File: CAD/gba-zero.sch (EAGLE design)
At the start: 35 parts, among them IC5 APX803, Q2 BSS138

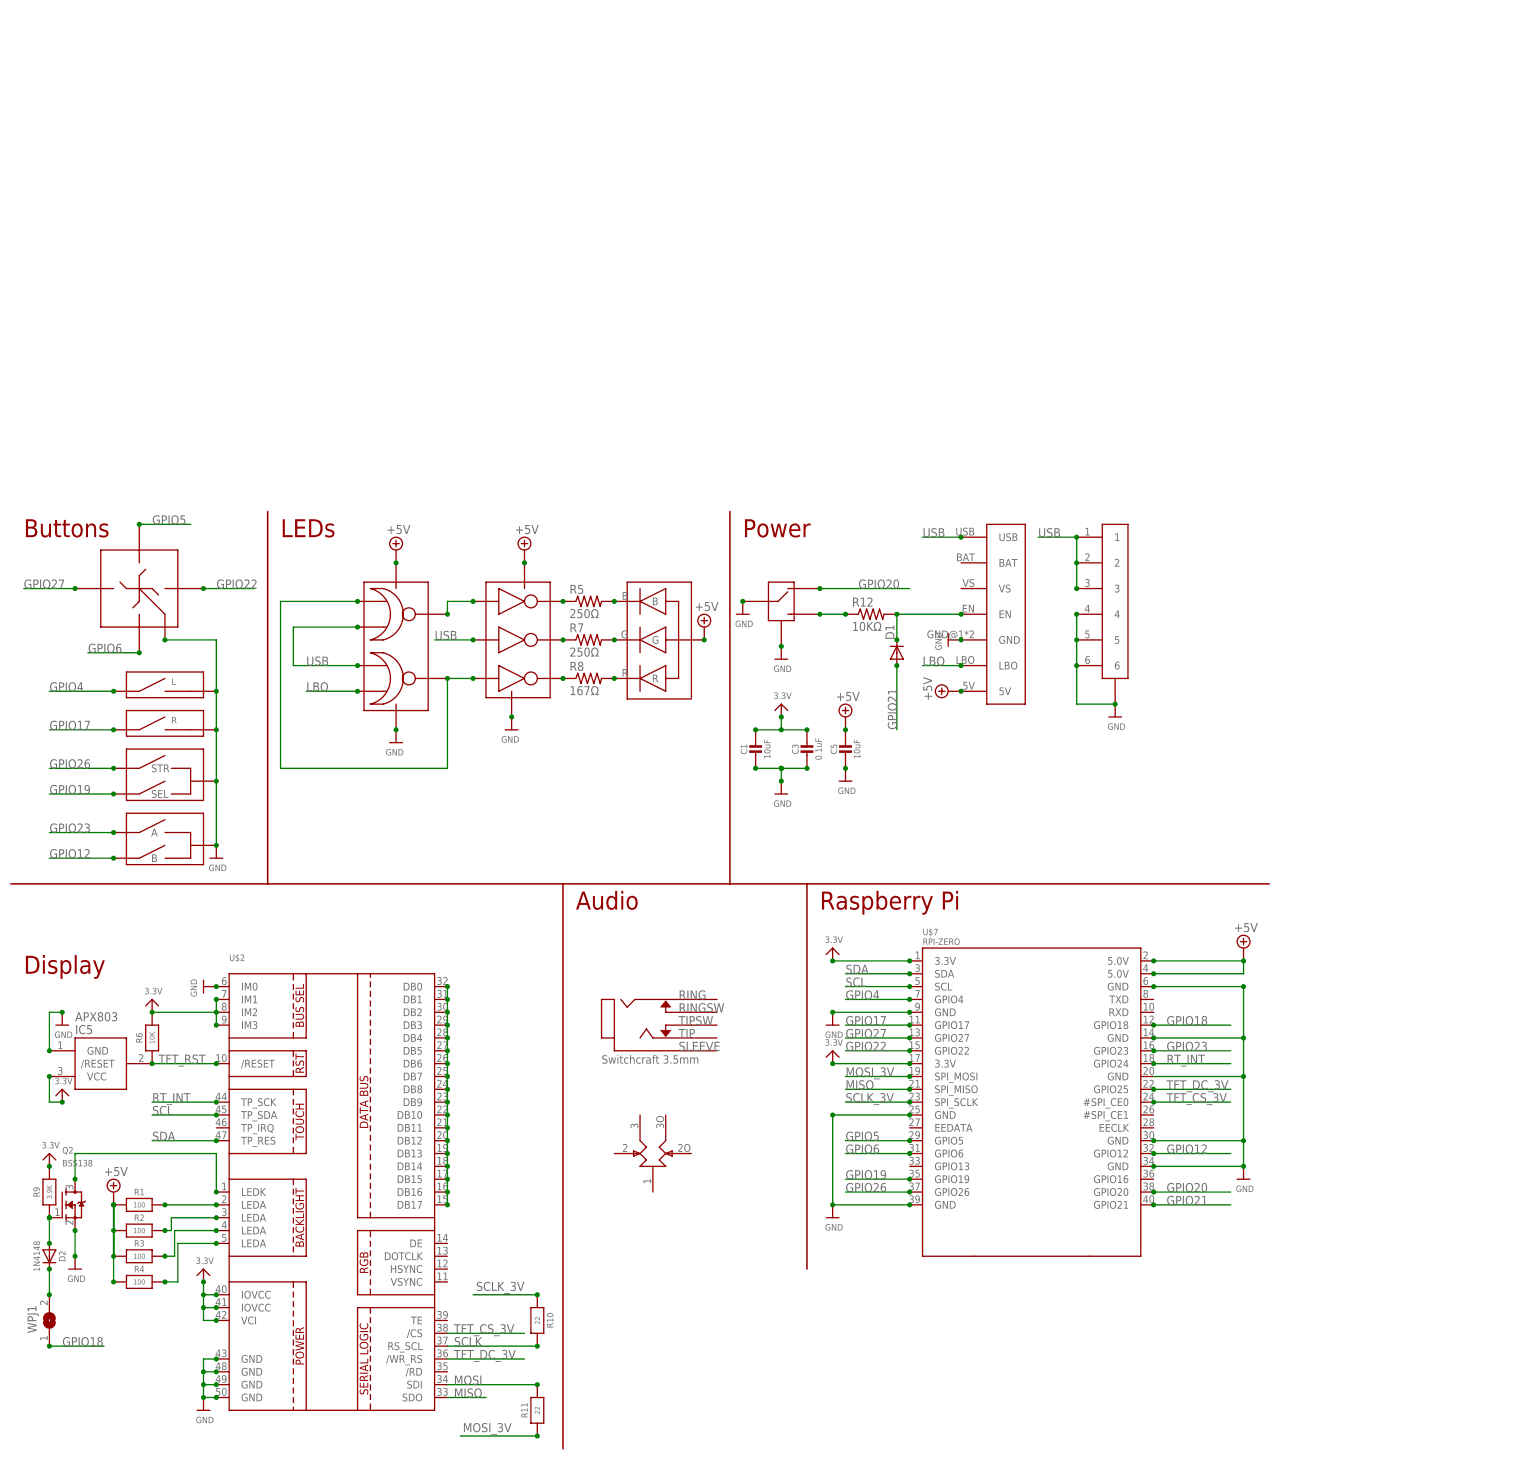
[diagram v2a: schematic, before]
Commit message: Added audio to schematic
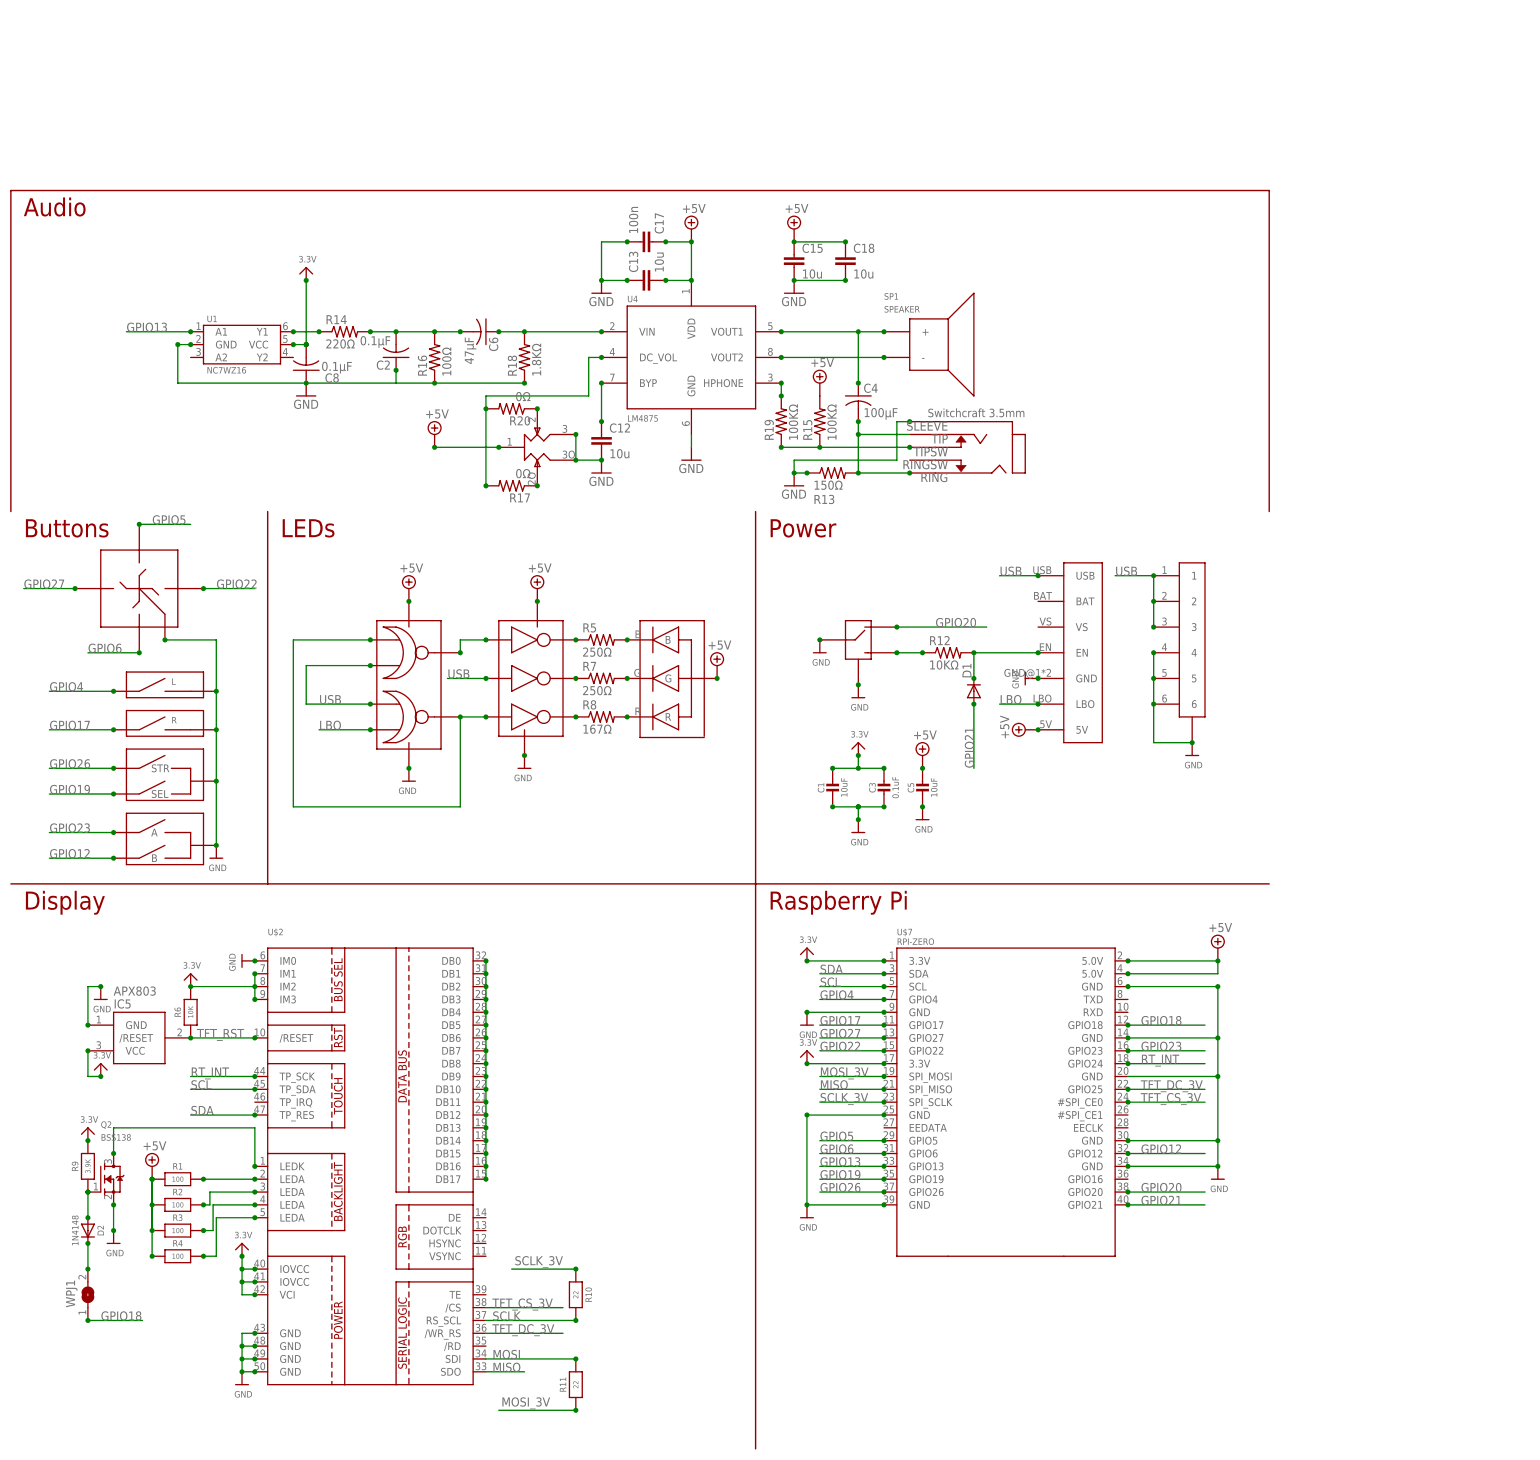
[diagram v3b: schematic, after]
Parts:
- removed U$15: RK10J12E0A0A, gba-zero-parts:RK10J12E0A0A
- removed U$22: SWTCHCRFT_3.5JACK5-JACK-SMD, gba-zero-parts:SWTCHCRFT_3.5JACK5-JACK-SMD
- added C12, C13, C15, C18: 10u, rcl:C-EUC0805
- added C17: 100n, rcl:C-EUC0805
- added C2, C8: 0.1μF, rcl:C-USC0603
- added C4: 100μF, rcl:C-USC0603
- added C6: 47μF, rcl:C-USC0603
- added R13: 150Ω, resistor:R-US_R0603
- added R14: 220Ω, resistor:R-US_R0603
- added R15, R19: 100KΩ, resistor:R-US_R0603
- added R16: 100Ω, resistor:R-US_R0603
- added R17, R20: 0Ω, resistor:R-US_R0603
- added R18: 1.8KΩ, resistor:R-US_R0603
- added SP1: SPEAKER, GBA:SPEAKER
- added U$16: SWTCHCRFT_3.5JACK5-JACK-SMD, gba-zero-parts:SWTCHCRFT_3.5JACK5-JACK-SMD
- added U$17: 10K, gba-zero-parts:RK10J12E0A0A
- added U1: NC7WZ16, fairchild:NC7WZ16
- added U4: LM4875, texas:LM4875
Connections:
- new net GPIO13: U$7.GPIO13, U1.A1
- new net N$19: C4.2, R13.2, U$16.2, U$16.3
- new net N$20: R14.1, U1.Y1
- new net N$21: C2.2, C6.2, R14.2, R16.2
- new net N$22: R15.1, R19.1, U$16.5
- new net N$23: R19.2, U4.HPHONE
- new net N$24: R17.1, U$17.2O
- new net N$25: R20.1, U$17.2
- new net N$26: R17.2, R20.2, U4.DC_VOL
- new net N$30: C6.1, R18.2, U4.VIN
- new net N$35: C12.1, U4.BYP
- new net N$36: C4.1, SP1.+, U4.VOUT1
- new net N$37: SP1.-, U4.VOUT2
- net +5V: now also C13.2, C15.1, C17.1, C18.1, R15.2, U$17.1, U4.VDD
- net 3.3V: now also C8.2, U1.VCC
- net GND: now also C12.2, C13.1, C15.2, C17.2, C18.2, C2.1, C8.1, R13.1, R16.1, R18.1, U$16.1, U$17.3, U$17.3O, U1.GND, U4.GND
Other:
- moved on the sheet: C1, C3, C5, D1, D2, IC5, Q2, R1, R10, R11, R12, R2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

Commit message: Lots of schematic cleanup
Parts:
- removed R13: 150Ω, resistor:R-US_R0603
- removed R14: 220Ω, resistor:R-US_R0603
- removed R15, R19: 100KΩ, resistor:R-US_R0603
- removed R16: 100Ω, resistor:R-US_R0603
- removed R18: 1.8KΩ, resistor:R-US_R0603
- added R21: 250, microbuilder:RESISTOR0805
- added R22, R23: 100K, microbuilder:RESISTOR0805
- added R24: 150, microbuilder:RESISTOR0805
- added WPJ4: 0, microbuilder:SOLDERJUMPERCLOSED
- C1, C3, C5: device microbuilder:CAP_CERAMIC0805-NOOUTLINE -> microbuilder:CAP_CERAMIC0805
- D1: value (none) -> IN4001
- R1, R10, R11, R2, R3, R4, R6, R9: device microbuilder:RESISTOR0805_NOOUTLINE -> microbuilder:RESISTOR0805
- R12: value 10KΩ -> 1.8K; device resistor:R-US_R0603 -> microbuilder:RESISTOR0805
- R17: value 0Ω -> 167; device resistor:R-US_R0603 -> microbuilder:RESISTOR0805
- R20: value 0Ω -> 250; device resistor:R-US_R0603 -> microbuilder:RESISTOR0805
- R5: value 250Ω -> 10K; device resistor:R-US_R0603 -> microbuilder:RESISTOR0805
- R7: value 250Ω -> 220; device resistor:R-US_R0603 -> microbuilder:RESISTOR0805
- R8: value 167Ω -> 100; device resistor:R-US_R0603 -> microbuilder:RESISTOR0805
- U$2: value (none) -> 50_PIN_CON
- U$7: device RPI-Zero:RPI-ZERO -> gba-zero-parts:RPI-ZERO
- WPJ1: value (none) -> 0
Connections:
- net GPIO12 renamed BTN_B
- net GPIO13 renamed AUD_PWM
- net GPIO17 renamed BTN_RS
- net GPIO18 renamed BKLT_PWM
- net GPIO19 renamed BTN_SEL
- net GPIO20 renamed PWR_SW_SEN
- net GPIO21 renamed PWR_EN_RPI
- net GPIO22 renamed BTN_R
- net GPIO23 renamed BTN_A
- net GPIO26 renamed BTN_STR
- net GPIO27 renamed BTN_L
- net GPIO4 renamed BTN_LS
- net GPIO5 renamed BTN_U
- net GPIO6 renamed BTN_D
- removed net 5.0V: C5.1, R1.1, R2.1, R3.1, R4.1, U$12.5V, U$42.VCC, U$43.VCC, U$44.VCC
- removed net N$19: C4.2, R13.2, U$16.2, U$16.3
- removed net N$24: R17.1, U$17.2O
- removed net N$25: R20.1, U$17.2
- new net BKLT: U$7.GPIO16, WPJ4.1
- new net RING: C4.2, R24.2, U$16.2, U$16.3
- new net RXD: U$10.3, U$7.RXD
- new net TXD: U$10.4, U$7.TXD
- net +5V: now also C5.P$1, R1.1, R2.1, R23.1, R3.1, R4.1, U$12.5V, U$42.VCC, U$43.VCC, U$44.VCC; no longer R15.2
- net 3.3V: now also C1.P$1, C3.P$1; no longer C1.1, C3.1
- net GND: now also C1.P$2, C3.P$2, C5.P$2, R12.2, R24.1, R8.2; no longer C1.2, C3.2, C5.2, R13.1, R16.1, R18.1, U$10.4
- net N$11: now also R20.2, U$43.2Y; no longer R8.1, U$43.3Y
- net N$12: now also R20.1, U$44.G; no longer R5.2, U$44.B
- net N$13: now also R21.2, U$43.1Y; no longer R7.2, U$44.G
- net N$14: now also R21.1, U$44.B; no longer R8.2, U$44.R
- net N$17: now also R5.2; no longer R12.1
- net N$18: now also R5.1; no longer R12.2
- net N$20: now also R7.2; no longer R14.1
- net N$21: now also R7.1, R8.1; no longer R14.2, R16.2
- net N$22: now also R22.2, R23.2; no longer R15.1, R19.1
- net N$23: now also R22.1; no longer R19.2
- net N$26: now also U$17.2; no longer R17.2, R20.2
- net N$30: now also R12.1; no longer R18.2
- net N$5: now also R17.2, U$43.3Y; no longer R5.1, U$43.1Y
- net N$6: now also WPJ4.2
- net N$8: now also R17.1, U$44.R; no longer R7.1, U$43.2Y
- net USB: no longer U$10.3
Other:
- moved on the sheet: C1, C2, C3, C5, C6, C8, D2, IC5, Q2, R1, R10, R11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

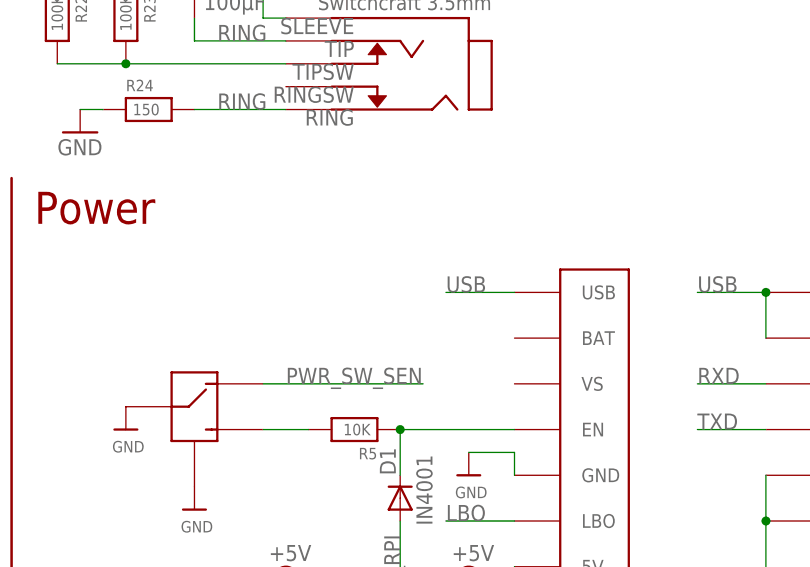
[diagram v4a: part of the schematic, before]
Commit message: Added JST battery connector
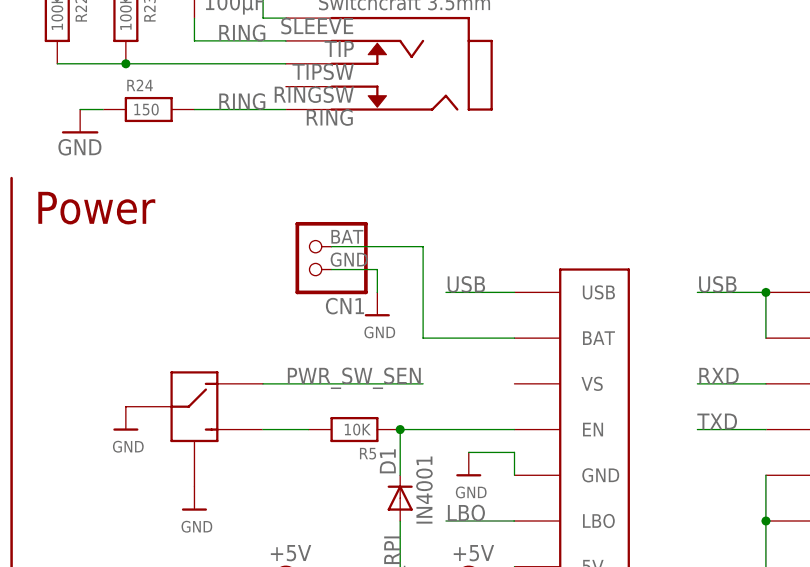
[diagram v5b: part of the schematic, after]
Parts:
- added CN1: (no value), gba-zero-parts:JST_2PIN
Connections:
- new net N$19: CN1.2, U$12.BAT
- net GND: now also CN1.1
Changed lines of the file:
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@@
 <setting verticaltext="up"/>
 </settings>
-<grid distance="0.1" unitdist="inch" unit="inch" style="lines" multiple="1" display="yes" altdistance="0.01" altunitdist="inch" altunit="inch"/>
+<grid distance="0.1" unitdist="inch" unit="inch" style="lines" multiple="1" display="no" altdistance="0.01" altunitdist="inch" altunit="inch"/>
 <layers>
 <layer number="1" name="Top" color="4" fill="1" visible="no" active="no"/>
@@
 <part name="R24" library="microbuilder" deviceset="RESISTOR" device="0805" value="150"/>
 <part name="GND3" library="SparkFun-Aesthetics" deviceset="GND" device=""/>
+<part name="CN1" library="gba-zero-parts" deviceset="JST_2PIN" device=""/>
+<part name="U$22" library="microbuilder" deviceset="GND" device=""/>
 </parts>
 <sheets>
@@
 </instance>
 <instance part="GND3" gate="1" x="177.8" y="208.28"/>
+<instance part="CN1" gate="G$1" x="180.34" y="177.8" rot="R180"/>
+<instance part="U$22" gate="G$1" x="187.96" y="170.18"/>
 </instances>
 <busses>
@@
 <pinref part="GND3" gate="1" pin="GND"/>
 <wire x1="175.26" y1="210.82" x2="177.8" y2="210.82" width="0.1524" layer="91"/>
+</segment>
+<segment>
+<pinref part="CN1" gate="G$1" pin="1"/>
+<pinref part="U$22" gate="G$1" pin="GND"/>
+<wire x1="182.88" y1="175.26" x2="187.96" y2="175.26" width="0.1524" layer="91"/>
+<wire x1="187.96" y1="175.26" x2="187.96" y2="172.72" width="0.1524" layer="91"/>
 </segment>
 </net>
@@
 </segment>
 </net>
+<net name="N$19" class="0">
+<segment>
+<pinref part="U$12" gate="G$1" pin="BAT"/>
+<wire x1="203.2" y1="167.64" x2="193.04" y2="167.64" width="0.1524" layer="91"/>
+<wire x1="193.04" y1="167.64" x2="193.04" y2="177.8" width="0.1524" layer="91"/>
+<pinref part="CN1" gate="G$1" pin="2"/>
+<wire x1="193.04" y1="177.8" x2="182.88" y2="177.8" width="0.1524" layer="91"/>
+</segment>
+</net>

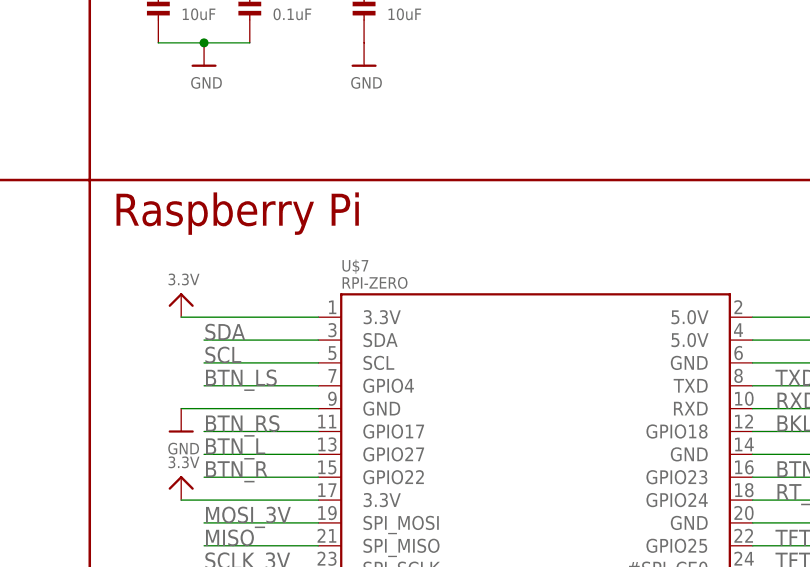
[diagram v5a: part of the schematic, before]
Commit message: Added new parts for SMD RPI, just the 510 pin FPC connector Sorted parts in the layout
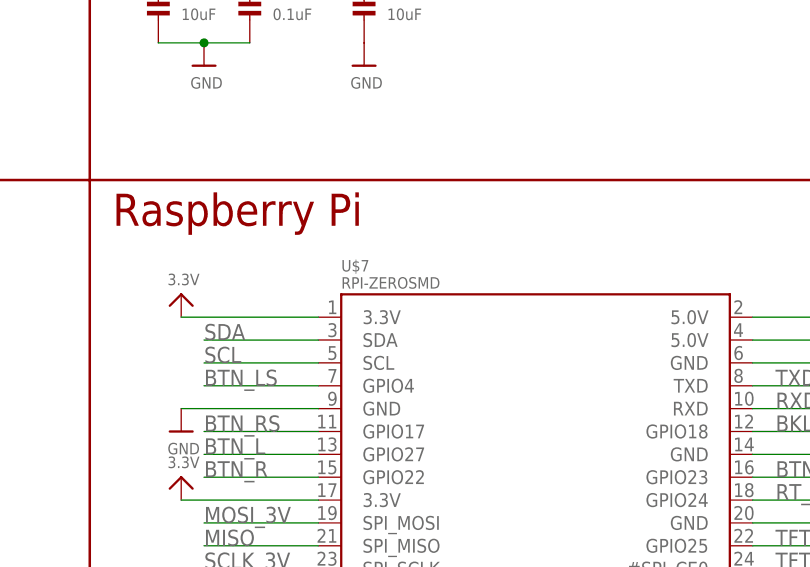
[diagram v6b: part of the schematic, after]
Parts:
- U$2: device gba-zero-parts:DISP_LCD_CTP28_SAMPLE -> gba-zero-parts:DISP_LCD_CTP28
- U$7: value RPI-ZERO -> RPI-ZEROSMD; device gba-zero-parts:RPI-ZERO -> gba-zero-parts:RPI-ZEROSMD
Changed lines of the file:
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@@
 <part name="U$14" library="microbuilder" deviceset="GND" device=""/>
 <part name="FRAME1" library="frames" deviceset="LETTER_L" device=""/>
-<part name="U$2" library="gba-zero-parts" deviceset="DISP_LCD_CTP28" device="_SAMPLE" value="50_PIN_CON"/>
+<part name="U$2" library="gba-zero-parts" deviceset="DISP_LCD_CTP28" device="" value="50_PIN_CON"/>
 <part name="U$8" library="microbuilder" deviceset="GND" device=""/>
 <part name="R6" library="microbuilder" deviceset="RESISTOR" device="0805" value="10K"/>
@@
 <part name="D2" library="microbuilder" deviceset="DIODE" device="SOD-323" value="1N4148"/>
 <part name="Q2" library="microbuilder" deviceset="MOSFET-N" device="WIDE" value="BSS138"/>
-<part name="U$7" library="gba-zero-parts" deviceset="RPI-ZERO" device=""/>
+<part name="U$7" library="gba-zero-parts" deviceset="RPI-ZERO" device="SMD" value="RPI-ZEROSMD"/>
 <part name="U$36" library="microbuilder" deviceset="GND" device=""/>
 <part name="U$38" library="microbuilder" deviceset="GND" device=""/>

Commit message: Added Ryzee's parts for placement
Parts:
- added D3: DUAL_LED, GBA:DUAL_LED
- added R13: 27k, GBA:VOLUME
- added SW1: LEFT, GBA:BUTTON
- added SW2: RIGHT, GBA:BUTTON
- added SW3: PWR_SWITCH, GBA:PWR_SWITCH
- added X1: LINK_SOCKET, GBA:LINK_SOCKET
- added X2: HEADPHONE, GBA:HEADPHONE
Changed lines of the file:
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@@
 <part name="CN1" library="gba-zero-parts" deviceset="JST_2PIN" device=""/>
 <part name="U$22" library="microbuilder" deviceset="GND" device=""/>
+<part name="X1" library="GBA" deviceset="LINK_SOCKET" device=""/>
+<part name="R13" library="GBA" deviceset="VOLUME" device="" value="27k"/>
+<part name="X2" library="GBA" deviceset="HEADPHONE" device=""/>
+<part name="SW1" library="GBA" deviceset="BUTTON" device="" value="LEFT"/>
+<part name="SW2" library="GBA" deviceset="BUTTON" device="" value="RIGHT"/>
+<part name="SW3" library="GBA" deviceset="PWR_SWITCH" device=""/>
+<part name="D3" library="GBA" deviceset="DUAL_LED" device=""/>
 </parts>
 <sheets>
@@
 <instance part="CN1" gate="G$1" x="180.34" y="177.8" rot="R180"/>
 <instance part="U$22" gate="G$1" x="187.96" y="170.18"/>
+<instance part="X1" gate="X$1" x="285.75" y="261.62" rot="MR90"/>
+<instance part="R13" gate="R$1" x="269.24" y="279.4"/>
+<instance part="X2" gate="X$1" x="276.86" y="243.84" rot="R180"/>
+<instance part="SW1" gate="SW$1" x="269.24" y="194.31" rot="R90"/>
+<instance part="SW2" gate="SW$1" x="279.4" y="193.04" rot="R90"/>
+<instance part="SW3" gate="SW$2" x="266.7" y="218.44" smashed="yes" rot="MR0">
+<attribute name="NAME" x="271.145" y="212.09" size="1.778" layer="95" rot="MR0"/>
+</instance>
+<instance part="D3" gate="D$1" x="270.51" y="154.94" rot="R90"/>
 </instances>
 <busses>
